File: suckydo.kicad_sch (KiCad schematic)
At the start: 76 parts, among them IC1 AP33771CFBZ-13-FA01, IC2 TS391SN2T1G, IC3 TPS561201DDCR, J1 HFW14R-1STE1H1LF, J2 USB4105-GF-A, Q1 PJA3404A, Q2 MMBT2222A, Q3 PJA3404A, Q5 MMBT2222A, Q6 PJA3404A, U1 ESP32-C6-MINI-1-H4

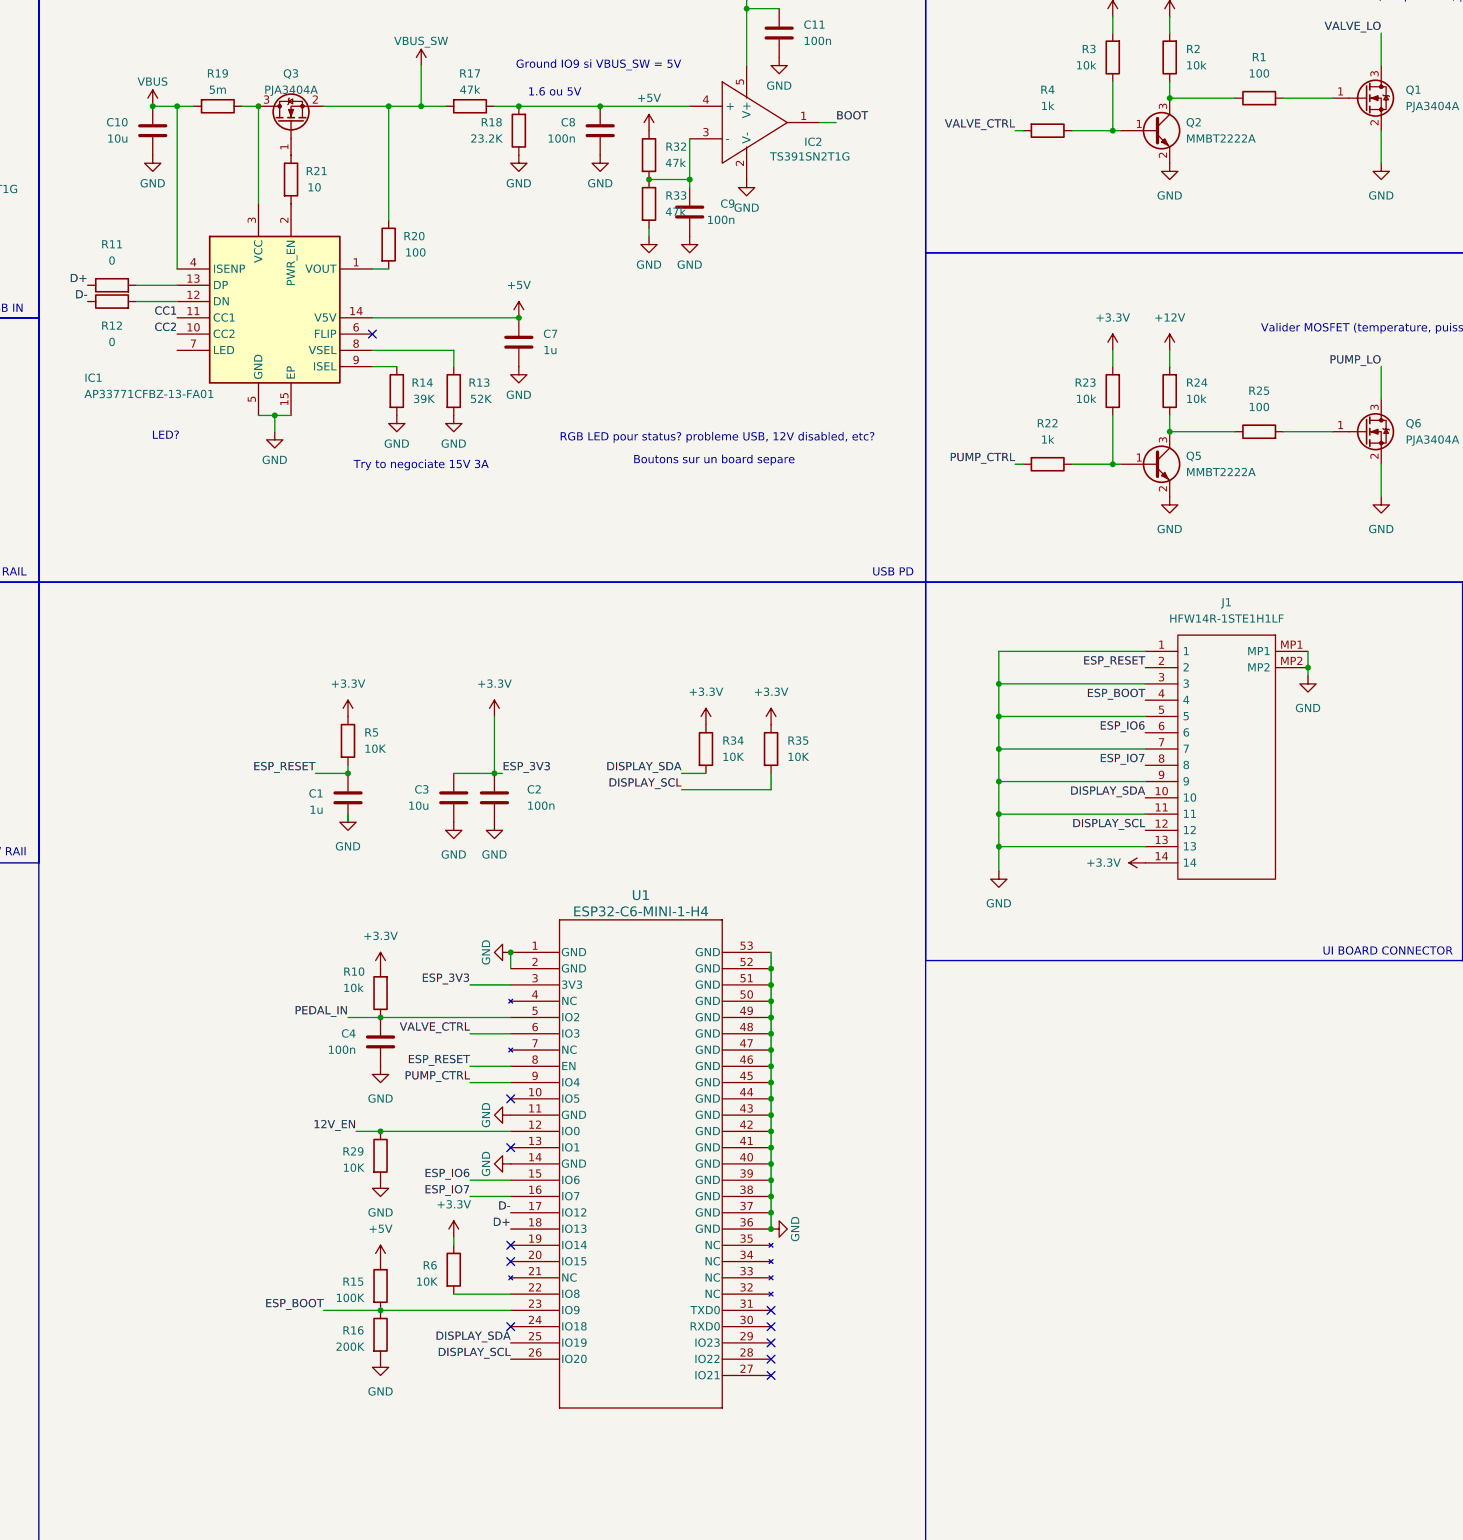
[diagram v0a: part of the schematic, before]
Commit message: status IOs
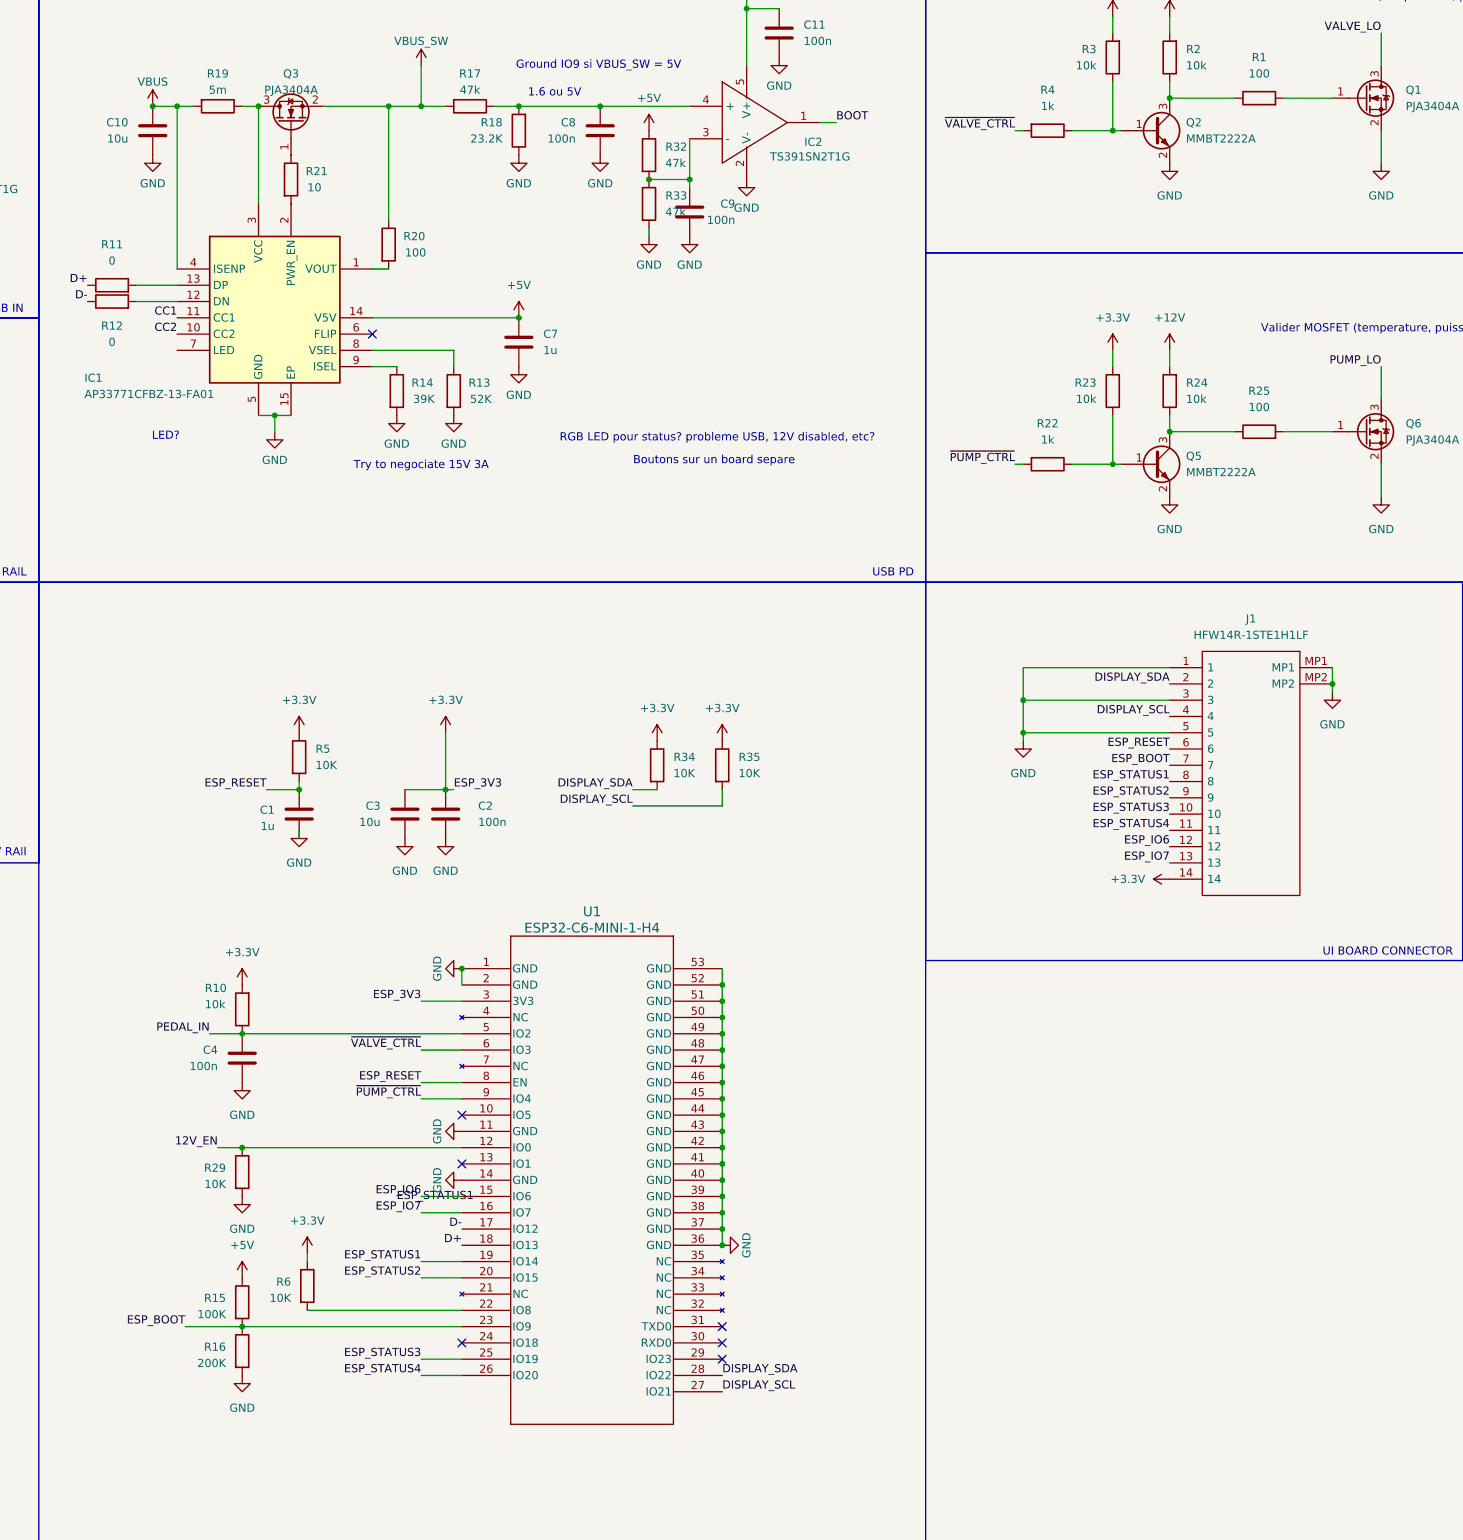
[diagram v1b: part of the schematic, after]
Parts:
- J1: footprint HFW14R1STE1H1LF -> Connector_FFC-FPC:HFW14R1STE1H1LF
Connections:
- net DISPLAY_SCL: now also J1.4, U1.27 (IO21); no longer J1.12, U1.26 (IO20)
- net DISPLAY_SDA: now also J1.2, U1.28 (IO22); no longer J1.10, U1.25 (IO19)
- net ESP_BOOT: now also J1.7; no longer J1.4
- net ESP_IO6: now also J1.12; no longer J1.6
- net ESP_IO7: now also J1.13; no longer J1.8
- net ESP_RESET: now also J1.6; no longer J1.2
- net GND: no longer J1.11, J1.13, J1.7, J1.9
- net ESP_STATUS1: now reaches U1.19 (IO14)
- net ESP_STATUS1: now also J1.8
- net ESP_STATUS2: now reaches U1.20 (IO15)
- net ESP_STATUS2: now also J1.9
- net PUMP_CTRL renamed ~{PUMP_CTRL}
- net VALVE_CTRL renamed ~{VALVE_CTRL}
- new net ESP_STATUS3: J1.10, U1.25 (IO19)
- new net ESP_STATUS4: J1.11, U1.26 (IO20)
- no-connect marks 13 -> 9
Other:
- moved on the sheet: C1, C2, C3, C4, J1, R10, R15, R16, R29, R34, R35, R5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

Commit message: footprints
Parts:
- IC1: footprint AP33771CFBZ13FA01 -> Package_DFN_QFN:AP33771CFBZ13FA01
- IC2: footprint SOT95P275X110-5N -> Package_TO_SOT_SMD:SOT95P275X110-5N
- IC3: footprint SOT95P280X110-6N -> Package_TO_SOT_SMD:SOT95P280X110-6N
- PS1: footprint TPS621361RGXT -> Package_DFN_QFN:TPS621361RGXT
- Pedal1: renamed from Pedal; footprint (none) -> TerminalBlock_TE-Connectivity:TerminalBlock_TE_282834-2_1x02_P2.54mm_Horizontal
- Pump1: renamed from Pump; footprint (none) -> TerminalBlock_TE-Connectivity:TerminalBlock_TE_282834-2_1x02_P2.54mm_Horizontal
- Valve1: renamed from Valve; footprint (none) -> TerminalBlock_TE-Connectivity:TerminalBlock_TE_282834-2_1x02_P2.54mm_Horizontal
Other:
- note added: "1.6V or 5V"
- note removed: "1.6 ou 5V"
- note removed: "Boutons sur un board separe"
- note removed: "Ground IO9 si VBUS_SW = 5V"
- note removed: "RGB LED pour status? probleme USB, 12V disabled, etc?"
- note removed: "Valider MOSFET (temperature, puissance)"
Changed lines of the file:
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@@
 	(wire
 		(pts
+			(xy 237.49 138.43) (xy 237.49 139.7)
+		)
+		(stroke
+			(width 0)
+			(type default)
+		)
+	)
+	(wire
+		(pts
 			(xy 39.37 90.17) (xy 39.37 92.71)
 		)
@@
 	(wire
 		(pts
+			(xy 247.65 138.43) (xy 247.65 139.7)
+		)
+		(stroke
+			(width 0)
+			(type default)
+		)
+	)
+	(wire
+		(pts
 			(xy 397.51 140.97) (xy 401.32 140.97)
 		)
@@
 		)
 	)
-	(text "Ground IO9 si VBUS_SW = 5V"
-		(exclude_from_sim no)
-		(at 228.346 34.29 0)
-		(effects
-			(font
-				(size 1.27 1.27)
-			)
-		)
-	)
 	(text "UI BOARD CONNECTOR"
 		(exclude_from_sim no)
@@
 		)
 	)
-	(text "Valider MOSFET (temperature, puissance)"
-		(exclude_from_sim no)
-		(at 350.012 75.438 0)
-		(effects
-			(font
-				(size 1.27 1.27)
-			)
-		)
-	)
 	(text "USB PD"
 		(exclude_from_sim no)
@@
 		)
 	)
-	(text "1.6 ou 5V"
+	(text "1.6V or 5V"
 		(exclude_from_sim no)
 		(at 221.488 38.608 0)
@@
 		)
 	)
-	(text "Valider MOSFET (temperature, puissance)"
-		(exclude_from_sim no)
-		(at 353.822 23.622 0)
-		(effects
-			(font
-				(size 1.27 1.27)
-			)
-		)
-	)
-	(text "Boutons sur un board separe"
-		(exclude_from_sim no)
-		(at 246.38 96.012 0)
-		(effects
-			(font
-				(size 1.27 1.27)
-			)
-		)
-	)
-	(text "RGB LED pour status? probleme USB, 12V disabled, etc?"
-		(exclude_from_sim no)
-		(at 246.888 92.456 0)
-		(effects
-			(font
-				(size 1.27 1.27)
-			)
-		)
-	)
 	(text "USB IN"
 		(exclude_from_sim no)
@@
 		(dnp no)
 		(fields_autoplaced yes)
-		(property "Reference" "Pedal"
+		(property "Reference" "Pedal1"
 			(at 408.94 140.9699 0)
 			(effects
@@
 			)
 		)
-		(property "Footprint" ""
+		(property "Footprint" "TerminalBlock_TE-Connectivity:TerminalBlock_TE_282834-2_1x02_P2.54mm_Horizontal"
 			(at 406.4 140.97 0)
 			(effects
@@
 			(project "suckydo"
 				(path "/c6a27179-ffbf-4c43-b356-2528cb51d20d"
-					(reference "Pedal")
+					(reference "Pedal1")
 					(unit 1)
 				)
@@
 			)
 		)
-		(property "Footprint" "TPS621361RGXT"
+		(property "Footprint" "Package_DFN_QFN:TPS621361RGXT"
 			(at 66.04 117.094 0)
 			(effects
@@
 	(symbol
 		(lib_id "power:+3.3V")
-		(at 247.65 139.7 0)
+		(at 247.65 138.43 0)
 		(unit 1)
 		(exclude_from_sim no)
@@
 		(fields_autoplaced yes)
 		(property "Reference" "#PWR071"
-			(at 247.65 143.51 0)
+			(at 247.65 142.24 0)
 			(effects
 				(font
@@
 		)
 		(property "Value" "+3.3V"
-			(at 247.65 134.62 0)
+			(at 247.65 133.35 0)
 			(effects
 				(font
@@
 		)
 		(property "Footprint" ""
-			(at 247.65 139.7 0)
+			(at 247.65 138.43 0)
 			(effects
 				(font
@@
 		)
 		(property "Datasheet" ""
-			(at 247.65 139.7 0)
+			(at 247.65 138.43 0)
 			(effects
 				(font
@@
 		)
 		(property "Description" "Power symbol creates a global label with name \"+3.3V\""
-			(at 247.65 139.7 0)
+			(at 247.65 138.43 0)
 			(effects
 				(font
@@
 			)
 		)
-		(property "Footprint" "SOT95P280X110-6N"
+		(property "Footprint" "Package_TO_SOT_SMD:SOT95P280X110-6N"
 			(at 74.93 187.63 0)
 			(effects
@@
 		(dnp no)
 		(fields_autoplaced yes)
-		(property "Reference" "Valve"
+		(property "Reference" "Valve1"
 			(at 408.94 38.0999 0)
 			(effects
@@
 			)
 		)
-		(property "Footprint" ""
+		(property "Footprint" "TerminalBlock_TE-Connectivity:TerminalBlock_TE_282834-2_1x02_P2.54mm_Horizontal"
 			(at 406.4 38.1 0)
 			(effects
@@
 			(project ""
 				(path "/c6a27179-ffbf-4c43-b356-2528cb51d20d"
-					(reference "Valve")
+					(reference "Valve1")
 					(unit 1)
 				)
@@
 			)
 		)
-		(property "Footprint" "SOT95P275X110-5N"
+		(property "Footprint" "Package_TO_SOT_SMD:SOT95P275X110-5N"
 			(at 273.05 129.21 0)
 			(effects
@@
 		(dnp no)
 		(fields_autoplaced yes)
-		(property "Reference" "Pump"
+		(property "Reference" "Pump1"
 			(at 408.94 90.1699 0)
 			(effects
@@
 			)
 		)
-		(property "Footprint" ""
+		(property "Footprint" "TerminalBlock_TE-Connectivity:TerminalBlock_TE_282834-2_1x02_P2.54mm_Horizontal"
 			(at 406.4 90.17 0)
 			(effects
@@
 			(project "suckydo"
 				(path "/c6a27179-ffbf-4c43-b356-2528cb51d20d"
-					(reference "Pump")
+					(reference "Pump1")
 					(unit 1)
 				)
@@
 	(symbol
 		(lib_id "power:+3.3V")
-		(at 237.49 139.7 0)
+		(at 237.49 138.43 0)
 		(unit 1)
 		(exclude_from_sim no)
@@
 		(fields_autoplaced yes)
 		(property "Reference" "#PWR070"
-			(at 237.49 143.51 0)
+			(at 237.49 142.24 0)
 			(effects
 				(font
@@
 		)
 		(property "Value" "+3.3V"
-			(at 237.49 134.62 0)
+			(at 237.49 133.35 0)
 			(effects
 				(font
@@
 		)
 		(property "Footprint" ""
-			(at 237.49 139.7 0)
+			(at 237.49 138.43 0)
 			(effects
 				(font
@@
 		)
 		(property "Datasheet" ""
-			(at 237.49 139.7 0)
+			(at 237.49 138.43 0)
 			(effects
 				(font
@@
 		)
 		(property "Description" "Power symbol creates a global label with name \"+3.3V\""
-			(at 237.49 139.7 0)
+			(at 237.49 138.43 0)
 			(effects
 				(font
@@
 			)
 		)
-		(property "Footprint" "AP33771CFBZ13FA01"
+		(property "Footprint" "Package_DFN_QFN:AP33771CFBZ13FA01"
 			(at 189.23 158.42 0)
 			(effects

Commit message: layout
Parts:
- Pedal1: value Screw_Terminal_01x02 -> Pedal
- Pump1: value Screw_Terminal_01x02 -> Pump
- R19, R7, R8: footprint Resistor_SMD:R_0402_1005Metric -> Resistor_SMD:R_0805_2012Metric
- Valve1: value Screw_Terminal_01x02 -> Valve
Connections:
- net DISPLAY_SCL: now also J1.2, U1.24 (IO18); no longer J1.4, U1.27 (IO21)
- net DISPLAY_SDA: now also J1.4, U1.25 (IO19); no longer J1.2, U1.28 (IO22)
- net ESP_STATUS1: now also J1.11, U1.28 (IO22); no longer J1.8, U1.19 (IO14)
- net ESP_STATUS2: now also J1.10, U1.29 (IO23); no longer J1.9, U1.20 (IO15)
- net ESP_STATUS3: now also J1.9, U1.30 (RXD0); no longer J1.10, U1.25 (IO19)
- net ESP_STATUS4: now also J1.8, U1.31 (TXD0); no longer J1.11, U1.26 (IO20)
- net PEDAL_IN: now also U1.20 (IO15); no longer U1.5 (IO2)
- net ESP_IO6: no longer names the net of U1.15 (IO6)
- net ESP_IO6: no longer J1.12
- net ESP_IO7: no longer names the net of U1.16 (IO7)
- net ESP_IO7: no longer J1.13
- new net ESP_IO20: J1.12, U1.26 (IO20)
- new net ESP_IO21: J1.13, U1.27 (IO21)
- no-connect marks 9 -> 5
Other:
- moved on the sheet: R6

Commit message: drc fixes
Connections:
- net +12V: now also Pump1.2 (Pin_2), Valve1.2 (Pin_2); no longer Pump1.1 (Pin_1), Valve1.1 (Pin_1)
- net GND: no longer J1.MP1, J1.MP2
- net PUMP_LO: now also Pump1.1 (Pin_1); no longer Pump1.2 (Pin_2)
- net VALVE_LO: now also Valve1.1 (Pin_1); no longer Valve1.2 (Pin_2)
- no-connect marks 5 -> 7
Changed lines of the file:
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@@
 	)
 	(junction
-		(at 342.9 130.81)
-		(diameter 0)
-		(color 0 0 0 0)
-	)
-	(junction
 		(at 308.61 96.52)
 		(diameter 0)
@@
 	)
 	(no_connect
+		(at 342.9 128.27)
+	)
+	(no_connect
 		(at 67.31 35.56)
 	)
@@
 	)
 	(no_connect
+		(at 342.9 130.81)
+	)
+	(no_connect
 		(at 193.04 76.2)
 	)
@@
 	(wire
 		(pts
-			(xy 401.32 87.63) (xy 391.16 87.63)
-		)
-		(stroke
-			(width 0)
-			(type default)
-		)
-	)
-	(wire
-		(pts
 			(xy 302.26 96.52) (xy 308.61 96.52)
 		)
@@
 	(wire
 		(pts
-			(xy 401.32 35.56) (xy 391.16 35.56)
+			(xy 207.01 223.52) (xy 199.39 223.52)
 		)
 		(stroke
@@
 	(wire
 		(pts
-			(xy 207.01 223.52) (xy 199.39 223.52)
+			(xy 401.32 35.56) (xy 391.16 35.56)
 		)
 		(stroke
@@
 	(wire
 		(pts
-			(xy 342.9 130.81) (xy 342.9 128.27)
-		)
-		(stroke
-			(width 0)
-			(type default)
-		)
-	)
-	(wire
-		(pts
 			(xy 198.12 147.32) (xy 204.47 147.32)
 		)
@@
 	(wire
 		(pts
-			(xy 342.9 132.08) (xy 342.9 130.81)
-		)
-		(stroke
-			(width 0)
-			(type default)
-		)
-	)
-	(wire
-		(pts
 			(xy 83.82 138.43) (xy 100.33 138.43)
 		)
@@
 	(wire
 		(pts
-			(xy 401.32 90.17) (xy 401.32 87.63)
-		)
-		(stroke
-			(width 0)
-			(type default)
-		)
-	)
-	(wire
-		(pts
 			(xy 200.66 40.64) (xy 195.58 40.64)
 		)
@@
 	(wire
 		(pts
-			(xy 401.32 38.1) (xy 401.32 35.56)
-		)
-		(stroke
-			(width 0)
-			(type default)
-		)
-	)
-	(wire
-		(pts
 			(xy 193.04 78.74) (xy 205.74 78.74)
 		)
@@
 	(wire
 		(pts
+			(xy 401.32 90.17) (xy 401.32 87.63)
+		)
+		(stroke
+			(width 0)
+			(type default)
+		)
+	)
+	(wire
+		(pts
 			(xy 350.52 29.21) (xy 350.52 34.29)
 		)
@@
 	(wire
 		(pts
+			(xy 401.32 38.1) (xy 401.32 35.56)
+		)
+		(stroke
+			(width 0)
+			(type default)
+		)
+	)
+	(wire
+		(pts
 			(xy 156.21 68.58) (xy 162.56 68.58)
 		)
@@
 	(wire
 		(pts
+			(xy 401.32 87.63) (xy 391.16 87.63)
+		)
+		(stroke
+			(width 0)
+			(type default)
+		)
+	)
+	(wire
+		(pts
 			(xy 247.65 185.42) (xy 247.65 187.96)
 		)
@@
 	(symbol
 		(lib_id "Connector:Screw_Terminal_01x02")
-		(at 406.4 38.1 0)
+		(at 406.4 40.64 0)
+		(mirror x)
 		(unit 1)
 		(exclude_from_sim no)
@@
 		(on_board yes)
 		(dnp no)
-		(fields_autoplaced yes)
 		(property "Reference" "Valve1"
-			(at 408.94 39.3699 0)
+			(at 408.94 39.3701 0)
 			(effects
 				(font
@@
 		)
 		(property "Value" "Valve"
-			(at 408.94 40.6399 0)
+			(at 408.94 38.1001 0)
 			(effects
 				(font
@@
 		)
 		(property "Footprint" "TerminalBlock_TE-Connectivity:TerminalBlock_TE_282834-2_1x02_P2.54mm_Horizontal"
-			(at 406.4 38.1 0)
+			(at 406.4 40.64 0)
 			(effects
 				(font
@@
 		)
 		(property "Datasheet" "~"
-			(at 406.4 38.1 0)
+			(at 406.4 40.64 0)
 			(effects
 				(font
@@
 		)
 		(property "Description" "Generic screw terminal, single row, 01x02, script generated (kicad-library-utils/schlib/autogen/connector/)"
-			(at 406.4 38.1 0)
+			(at 406.4 40.64 0)
 			(effects
 				(font
@@
 	(symbol
 		(lib_id "Connector:Screw_Terminal_01x02")
-		(at 406.4 90.17 0)
+		(at 406.4 92.71 0)
+		(mirror x)
 		(unit 1)
 		(exclude_from_sim no)
@@
 		(on_board yes)
 		(dnp no)
-		(fields_autoplaced yes)
 		(property "Reference" "Pump1"
-			(at 408.94 91.4399 0)
+			(at 408.94 91.4401 0)
 			(effects
 				(font
@@
 		)
 		(property "Value" "Pump"
-			(at 408.94 92.7099 0)
+			(at 408.94 90.1701 0)
 			(effects
 				(font
@@
 		)
 		(property "Footprint" "TerminalBlock_TE-Connectivity:TerminalBlock_TE_282834-2_1x02_P2.54mm_Horizontal"
-			(at 406.4 90.17 0)
+			(at 406.4 92.71 0)
 			(effects
 				(font
@@
 		)
 		(property "Datasheet" "~"
-			(at 406.4 90.17 0)
+			(at 406.4 92.71 0)
 			(effects
 				(font
@@
 		)
 		(property "Description" "Generic screw terminal, single row, 01x02, script generated (kicad-library-utils/schlib/autogen/connector/)"
-			(at 406.4 90.17 0)
+			(at 406.4 92.71 0)
 			(effects
 				(font
@@
 					(unit 1)
 				)
-			)
-		)
-	)
-	(symbol
-		(lib_id "power:GND")
-		(at 342.9 132.08 0)
-		(unit 1)
-		(exclude_from_sim no)
-		(in_bom yes)
-		(on_board yes)
-		(dnp no)
-		(fields_autoplaced yes)
-		(property "Reference" "#PWR054"
-			(at 342.9 138.43 0)
-			(effects
-				(font
-					(size 1.27 1.27)
-				)
-				(hide yes)
-			)
-		)
-		(property "Value" "GND"
-			(at 342.9 137.16 0)
-			(effects
-				(font
-					(size 1.27 1.27)
-				)
-			)
-		)
-		(property "Footprint" ""
-			(at 342.9 132.08 0)
-			(effects
-				(font
-					(size 1.27 1.27)
-				)
-				(hide yes)
-			)
-		)
-		(property "Datasheet" ""
-			(at 342.9 132.08 0)
-			(effects
-				(font
-					(size 1.27 1.27)
-				)
-				(hide yes)
-			)
-		)
-		(property "Description" ""
-			(at 342.9 132.08 0)
-			(effects
-				(font
-					(size 1.27 1.27)
-				)
-				(hide yes)
-			)
-		)
-		(pin "1"
-		)
-		(instances
-			(project "suckydo"
-				(path "/c6a27179-ffbf-4c43-b356-2528cb51d20d"
-					(reference "#PWR054")
-					(unit 1)
-				)
